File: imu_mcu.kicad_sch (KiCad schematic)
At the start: 11 parts, among them SW1 SW_Push, SW2 SW_Push, U4 ESP32-C3-WROOM-02

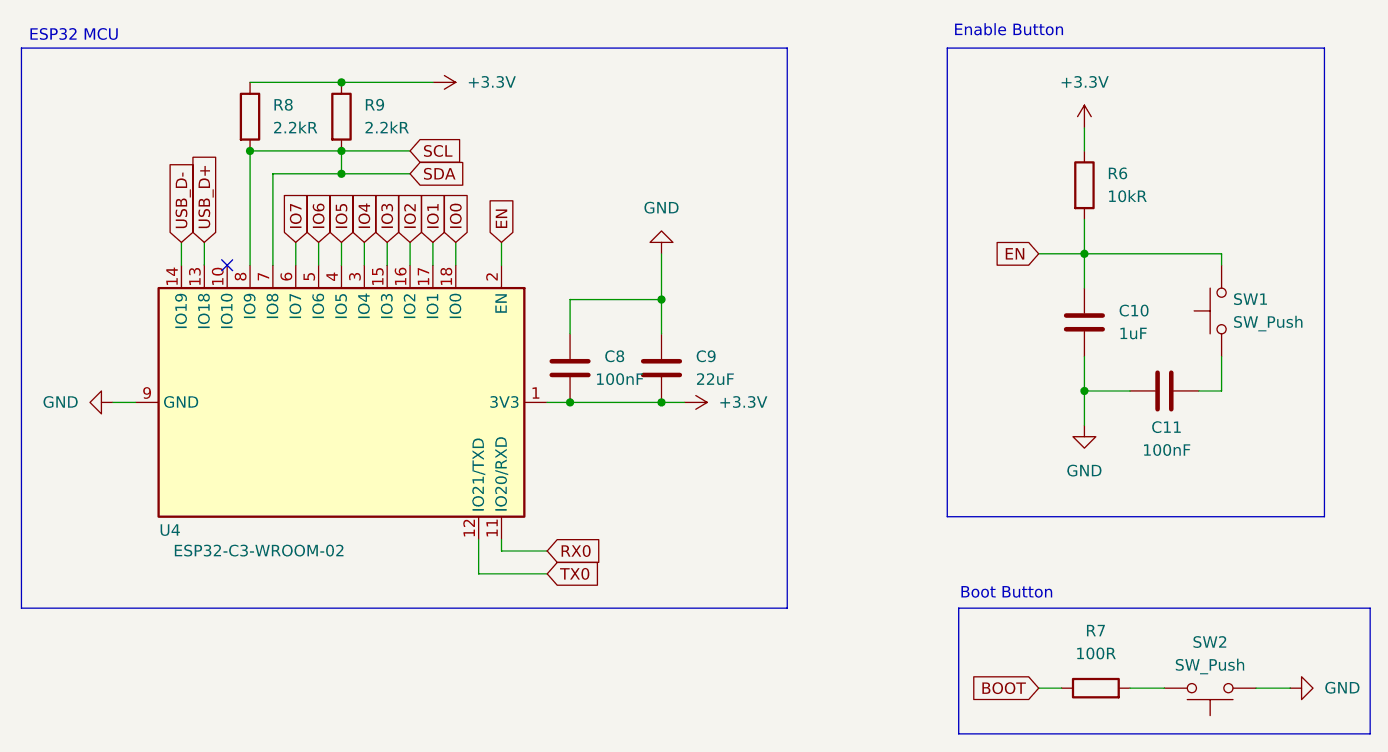
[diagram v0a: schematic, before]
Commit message: Route Traces for ESP32 and related IO
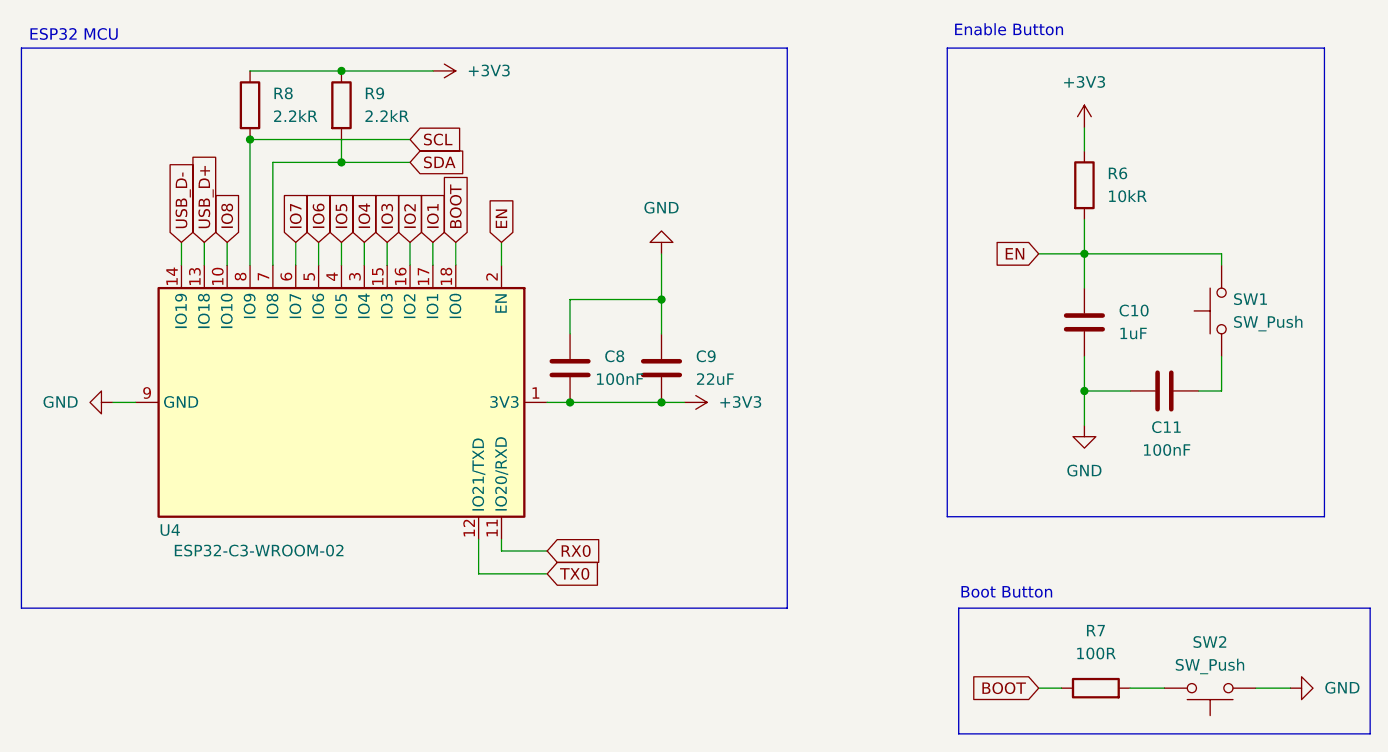
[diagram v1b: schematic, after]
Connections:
- net IO0 is gone; now on net BOOT: U4.18 (IO0)
- net SCL: no longer R9.2, U4.7 (IO8)
- net IO8: now reaches U4.10 (IO10)
- net +3.3V renamed +3V3
- new net SDA: R9.2, U4.7 (IO8)
- no-connect marks 1 -> 0
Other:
- moved on the sheet: R8, R9
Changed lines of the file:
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@@
-	)
-	(junction
-		(at 105.41 67.31)
-		(diameter 0)
-		(color 0 0 0 0)
 	)
 	(junction
@@
 	)
 	(junction
-		(at 105.41 69.85)
+		(at 105.41 68.58)
 		(diameter 0)
 		(color 0 0 0 0)
@@
 	)
 	(junction
-		(at 95.25 67.31)
+		(at 95.25 66.04)
 		(diameter 0)
 		(color 0 0 0 0)
@@
 	)
 	(junction
-		(at 105.41 59.69)
+		(at 105.41 58.42)
 		(diameter 0)
 		(color 0 0 0 0)
 	)
-	(no_connect
-		(at 92.71 80.01)
-	)
-	(wire
-		(pts
-			(xy 105.41 69.85) (xy 113.03 69.85)
-		)
-		(stroke
-			(width 0)
-			(type default)
-		)
-	)
-	(wire
-		(pts
-			(xy 105.41 67.31) (xy 105.41 69.85)
+	(wire
+		(pts
+			(xy 105.41 68.58) (xy 113.03 68.58)
+		)
+		(stroke
+			(width 0)
+			(type default)
+		)
+	)
+	(wire
+		(pts
+			(xy 105.41 66.04) (xy 105.41 68.58)
 		)
 		(stroke
@@
 	(wire
 		(pts
-			(xy 105.41 67.31) (xy 113.03 67.31)
-		)
-		(stroke
-			(width 0)
-			(type default)
-		)
-	)
-	(wire
-		(pts
-			(xy 95.25 80.01) (xy 95.25 67.31)
+			(xy 92.71 77.47) (xy 92.71 80.01)
+		)
+		(stroke
+			(width 0)
+			(type default)
+		)
+	)
+	(wire
+		(pts
+			(xy 95.25 66.04) (xy 113.03 66.04)
 		)
 		(stroke
@@
 	(wire
 		(pts
-			(xy 105.41 59.69) (xy 115.57 59.69)
-		)
-		(stroke
-			(width 0)
-			(type default)
-		)
-	)
-	(wire
-		(pts
-			(xy 97.79 80.01) (xy 97.79 69.85)
-		)
-		(stroke
-			(width 0)
-			(type default)
-		)
-	)
-	(wire
-		(pts
-			(xy 95.25 67.31) (xy 105.41 67.31)
+			(xy 105.41 58.42) (xy 115.57 58.42)
+		)
+		(stroke
+			(width 0)
+			(type default)
+		)
+	)
+	(wire
+		(pts
+			(xy 95.25 66.04) (xy 95.25 80.01)
 		)
 		(stroke
@@
 	(wire
 		(pts
+			(xy 97.79 68.58) (xy 97.79 80.01)
+		)
+		(stroke
+			(width 0)
+			(type default)
+		)
+	)
+	(wire
+		(pts
 			(xy 123.19 77.47) (xy 123.19 80.01)
 		)
@@
 	(wire
 		(pts
-			(xy 95.25 59.69) (xy 105.41 59.69)
+			(xy 95.25 58.42) (xy 105.41 58.42)
 		)
 		(stroke
@@
 	(wire
 		(pts
-			(xy 97.79 69.85) (xy 105.41 69.85)
+			(xy 97.79 68.58) (xy 105.41 68.58)
 		)
 		(stroke
@@
 	(global_label "SDA"
 		(shape input)
-		(at 113.03 69.85 0)
+		(at 113.03 68.58 0)
 		(fields_autoplaced yes)
 		(effects
@@
 		)
 		(property "Intersheetrefs" "${INTERSHEET_REFS}"
-			(at 119.5833 69.85 0)
+			(at 119.5833 68.58 0)
+			(effects
+				(font
+					(size 1.27 1.27)
+				)
+				(justify left)
+				(hide yes)
+			)
+		)
+	)
+	(global_label "IO8"
+		(shape input)
+		(at 92.71 77.47 90)
+		(fields_autoplaced yes)
+		(effects
+			(font
+				(size 1.27 1.27)
+			)
+			(justify left)
+		)
+		(property "Intersheetrefs" "${INTERSHEET_REFS}"
+			(at 92.71 71.34 90)
 			(effects
 				(font
@@
 		)
 	)
-	(global_label "IO0"
+	(global_label "BOOT"
 		(shape input)
 		(at 118.11 77.47 90)
@@
 		)
 		(property "Intersheetrefs" "${INTERSHEET_REFS}"
-			(at 118.11 71.34 90)
+			(at 118.11 69.5862 90)
 			(effects
 				(font
@@
 	(global_label "SCL"
 		(shape input)
-		(at 113.03 67.31 0)
+		(at 113.03 66.04 0)
 		(fields_autoplaced yes)
 		(effects
@@
 		)
 		(property "Intersheetrefs" "${INTERSHEET_REFS}"
-			(at 119.5228 67.31 0)
+			(at 119.5228 66.04 0)
 			(effects
 				(font
@@
 	(symbol
 		(lib_id "power:+3.3V")
-		(at 115.57 59.69 270)
+		(at 115.57 58.42 270)
 		(unit 1)
 		(exclude_from_sim no)
@@
 		(fields_autoplaced yes)
 		(property "Reference" "#PWR036"
-			(at 111.76 59.69 0)
-			(effects
-				(font
-					(size 1.27 1.27)
-				)
-				(hide yes)
-			)
-		)
-		(property "Value" "+3.3V"
-			(at 119.38 59.6899 90)
+			(at 111.76 58.42 0)
+			(effects
+				(font
+					(size 1.27 1.27)
+				)
+				(hide yes)
+			)
+		)
+		(property "Value" "+3V3"
+			(at 119.38 58.4199 90)
 			(effects
 				(font
@@
 		)
 		(property "Footprint" ""
-			(at 115.57 59.69 0)
+			(at 115.57 58.42 0)
 			(effects
 				(font
@@
 		)
 		(property "Datasheet" ""
-			(at 115.57 59.69 0)
+			(at 115.57 58.42 0)
 			(effects
 				(font
@@
 		)
 		(property "Description" "Power symbol creates a global label with name \"+3.3V\""
-			(at 115.57 59.69 0)
+			(at 115.57 58.42 0)
 			(effects
 				(font
@@
 			)
 		)
-		(property "Value" "+3.3V"
+		(property "Value" "+3V3"
 			(at 187.96 59.69 0)
 			(effects
@@
 	(symbol
 		(lib_id "Device:R")
-		(at 105.41 63.5 0)
+		(at 105.41 62.23 0)
 		(unit 1)
 		(exclude_from_sim no)
@@
 		(fields_autoplaced yes)
 		(property "Reference" "R9"
-			(at 107.95 62.2299 0)
+			(at 107.95 60.9599 0)
 			(effects
 				(font
@@
 		)
 		(property "Value" "2.2kR"
-			(at 107.95 64.7699 0)
+			(at 107.95 63.4999 0)
 			(effects
 				(font
@@
 		)
 		(property "Footprint" "Resistor_SMD:R_0805_2012Metric_Pad1.20x1.40mm_HandSolder"
-			(at 103.632 63.5 90)
+			(at 103.632 62.23 90)
 			(effects
 				(font
@@
 		)
 		(property "Datasheet" "~"
-			(at 105.41 63.5 0)
+			(at 105.41 62.23 0)
 			(effects
 				(font
@@
 		)
 		(property "Description" "Resistor"
-			(at 105.41 63.5 0)
+			(at 105.41 62.23 0)
 			(effects
 				(font
@@
 	(symbol
 		(lib_id "Device:R")
-		(at 95.25 63.5 0)
+		(at 95.25 62.23 0)
 		(unit 1)
 		(exclude_from_sim no)
@@
 		(fields_autoplaced yes)
 		(property "Reference" "R8"
-			(at 97.79 62.2299 0)
+			(at 97.79 60.9599 0)
 			(effects
 				(font
@@
 		)
 		(property "Value" "2.2kR"
-			(at 97.79 64.7699 0)
+			(at 97.79 63.4999 0)
 			(effects
 				(font
@@
 		)
 		(property "Footprint" "Resistor_SMD:R_0805_2012Metric_Pad1.20x1.40mm_HandSolder"
-			(at 93.472 63.5 90)
+			(at 93.472 62.23 90)
 			(effects
 				(font
@@
 		)
 		(property "Datasheet" "~"
-			(at 95.25 63.5 0)
+			(at 95.25 62.23 0)
 			(effects
 				(font
@@
 		)
 		(property "Description" "Resistor"
-			(at 95.25 63.5 0)
+			(at 95.25 62.23 0)
 			(effects
 				(font
@@
 			)
 		)
-		(property "Value" "+3.3V"
+		(property "Value" "+3V3"
 			(at 147.32 95.2499 90)
 			(effects

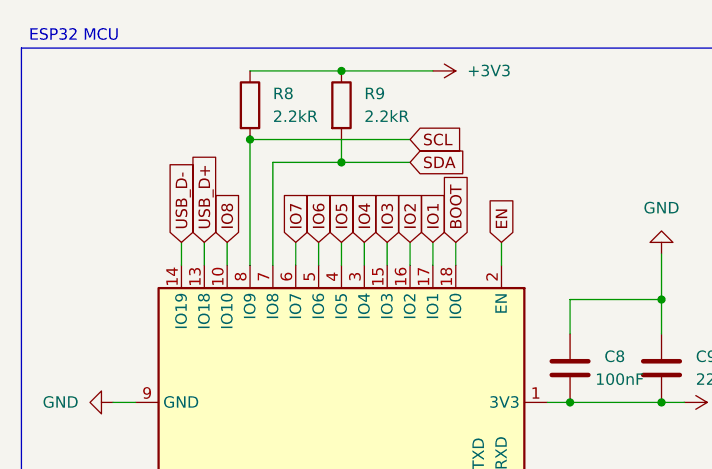
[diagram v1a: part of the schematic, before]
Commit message: Add Sensors and Silkscreen Adjustments
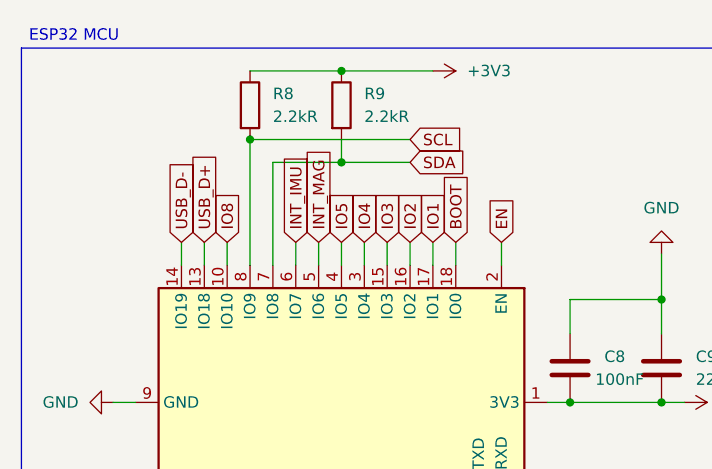
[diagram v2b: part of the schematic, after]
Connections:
- net IO6 renamed INT_MAG
- net IO7 renamed INT_IMU
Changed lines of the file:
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@@
-		)
-	)
-	(global_label "IO7"
-		(shape input)
-		(at 100.33 77.47 90)
-		(fields_autoplaced yes)
-		(effects
-			(font
-				(size 1.27 1.27)
-			)
-			(justify left)
-		)
-		(property "Intersheetrefs" "${INTERSHEET_REFS}"
-			(at 100.33 71.34 90)
-			(effects
-				(font
-					(size 1.27 1.27)
-				)
-				(justify left)
-				(hide yes)
-			)
 		)
 	)
@@
 		(property "Intersheetrefs" "${INTERSHEET_REFS}"
 			(at 115.57 71.34 90)
+			(effects
+				(font
+					(size 1.27 1.27)
+				)
+				(justify left)
+				(hide yes)
+			)
+		)
+	)
+	(global_label "INT_MAG"
+		(shape input)
+		(at 102.87 77.47 90)
+		(fields_autoplaced yes)
+		(effects
+			(font
+				(size 1.27 1.27)
+			)
+			(justify left)
+		)
+		(property "Intersheetrefs" "${INTERSHEET_REFS}"
+			(at 102.87 66.8043 90)
 			(effects
 				(font
@@
 		)
 	)
-	(global_label "IO6"
-		(shape input)
-		(at 102.87 77.47 90)
-		(fields_autoplaced yes)
-		(effects
-			(font
-				(size 1.27 1.27)
-			)
-			(justify left)
-		)
-		(property "Intersheetrefs" "${INTERSHEET_REFS}"
-			(at 102.87 71.34 90)
-			(effects
-				(font
-					(size 1.27 1.27)
-				)
-				(justify left)
-				(hide yes)
-			)
-		)
-	)
 	(global_label "BOOT"
 		(shape input)
@@
 			(effects
 				(font
+					(size 1.27 1.27)
+				)
+				(justify left)
+				(hide yes)
+			)
+		)
+	)
+	(global_label "INT_IMU"
+		(shape input)
+		(at 100.33 77.47 90)
+		(fields_autoplaced yes)
+		(effects
+			(font
+				(size 1.27 1.27)
+			)
+			(justify left)
+		)
+		(property "Intersheetrefs" "${INTERSHEET_REFS}"
+			(at 100.33 67.2276 90)
+			(effects
+				(font
